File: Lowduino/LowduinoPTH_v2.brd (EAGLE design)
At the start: 17.8 x 54.6 mm, 23 parts, among them Q1 32.768kHz, U1 ATMEGA328P_PDIP

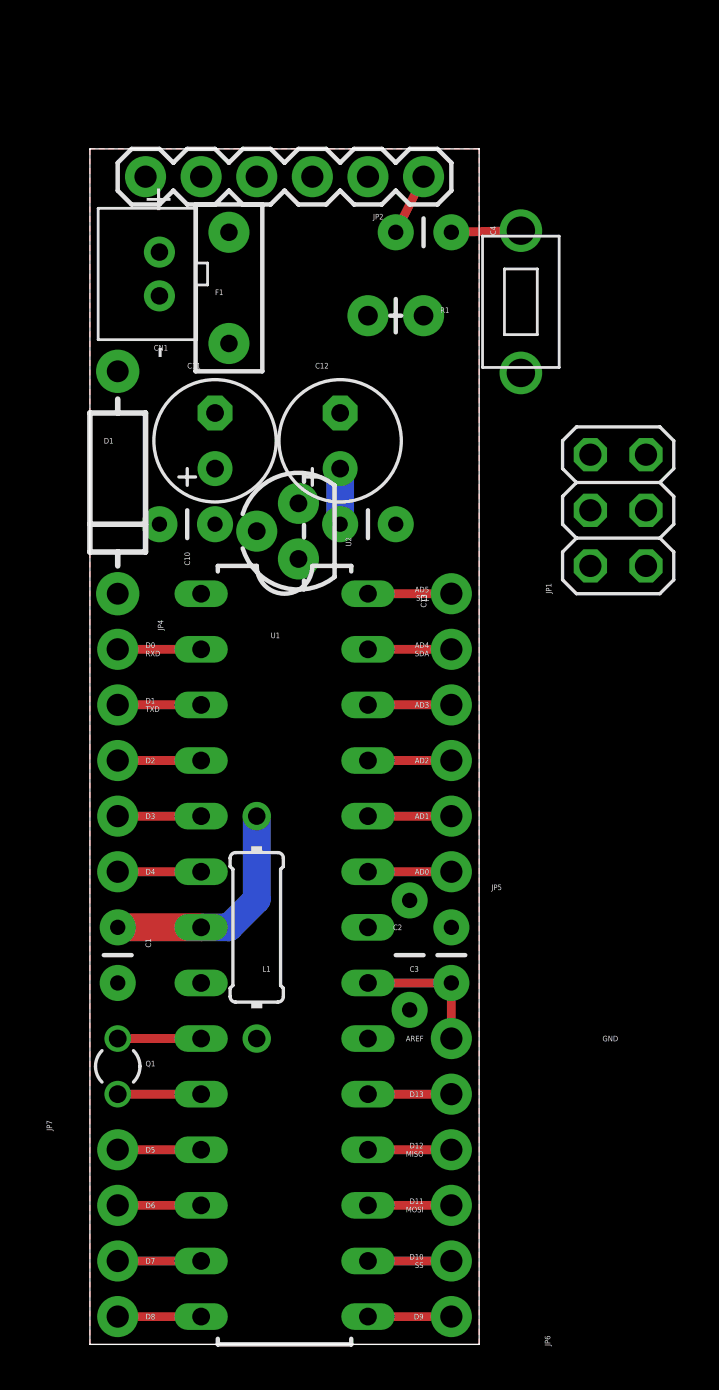
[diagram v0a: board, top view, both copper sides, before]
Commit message: Moved 1V8 voltage regulators from DensityAltitude.lbr to 1V8.lbr More layout work for various high input voltage regulators A bit more work on LowduinoPTH_v2
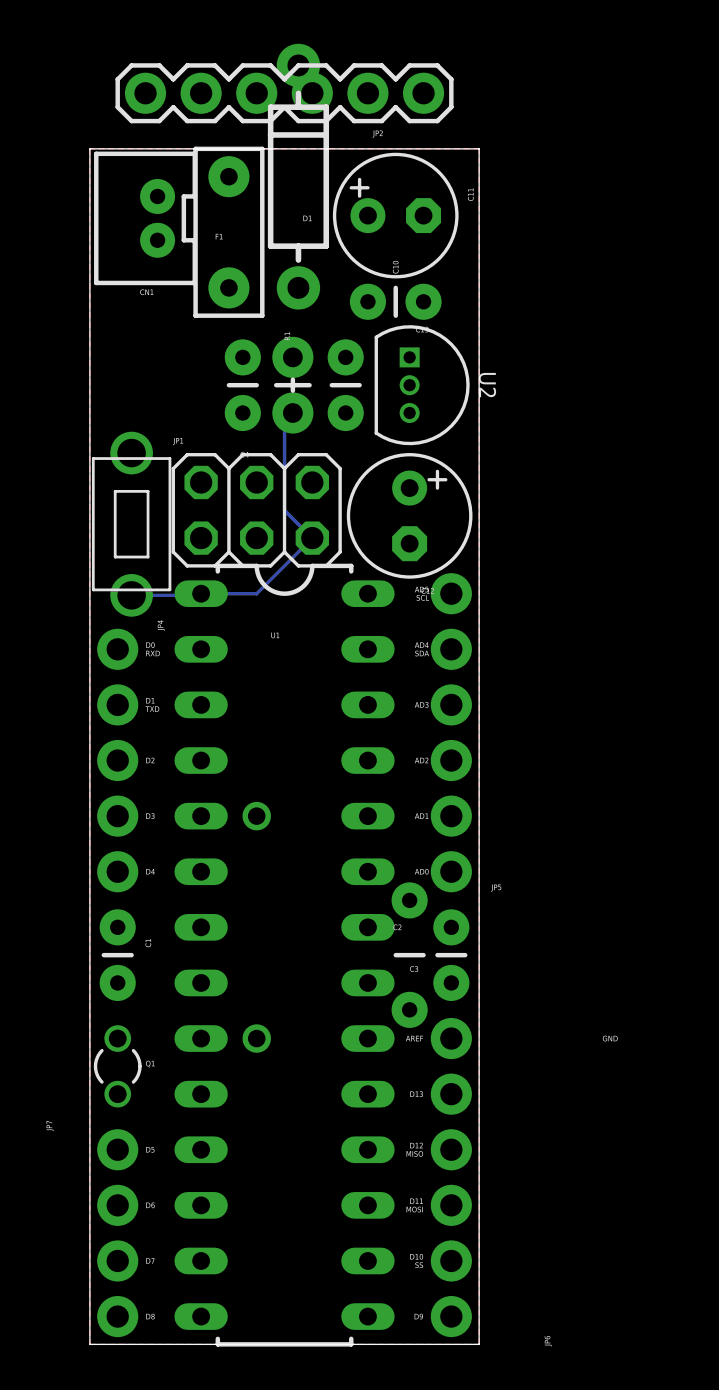
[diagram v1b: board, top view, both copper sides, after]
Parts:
- CN1: device adafruit:JST-PH-2-THM -> SparkFun-Connectors:JST-2-PTH-VERT
- U2: value (none) -> MCP1700-1802E/TO; device SparkFun-PowerIC:TO-92 -> 1V8:MICROCHIP_TO
- moved S1 20.5 mm to (1.91, 37.5), turned to 270 degrees
- moved JP1 16.5 mm to (7.62, 38.1), turned to 0 degrees
- moved D1 16.2 mm to (9.53, 53.3), turned to 90 degrees
- moved C11 13.2 mm to (14.0, 51.6), turned to 0 degrees
- moved C10 12.3 mm to (12.7, 47.6), turned to 0 degrees
- moved C4 9.03 mm to (6.99, 45.1), turned to 270 degrees
- moved U2 8.38 mm to (14.6, 43.8), turned to 270 degrees
- moved R1 5.61 mm to (9.27, 42.5), turned to 90 degrees
- moved C13 5.09 mm to (11.7, 42.5), turned to 90 degrees
- moved C12 4.67 mm to (14.6, 37.8), turned to 270 degrees
- moved JP2 3.81 mm to (15.2, 57.1)
- moved CN1 2.62 mm to (2.54, 51.4)
- moved F1 2.54 mm to (6.35, 50.8)
- flipped L1 to the bottom
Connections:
- net GND: now also CN1.1; no longer CN1.2
- net VIN: now also CN1.2; no longer CN1.1
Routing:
- net 1.8V: track 13.2 -> 0.00 mm
- net !RESET: track 3.18 -> 15.7 mm
- net AREF: track 6.35 -> 0.00 mm
- net D9: track 3.81 -> 0.00 mm
- net D13/SCK: track 3.81 -> 0.00 mm
- net D12/MISO: track 3.81 -> 0.00 mm
- net D11/MOSI: track 3.81 -> 0.00 mm
- net D10/SS: track 3.81 -> 0.00 mm
- net AD5/SCL: track 3.81 -> 0.00 mm
- net AD4/SDA: track 3.81 -> 0.00 mm
- net AD3: track 3.81 -> 0.00 mm
- net AD2: track 3.81 -> 0.00 mm
- net AD1: track 3.81 -> 0.00 mm
- net AD0: track 3.81 -> 0.00 mm
- net XTAL2: track 3.81 -> 0.00 mm
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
